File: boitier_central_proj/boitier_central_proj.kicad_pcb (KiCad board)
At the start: 2 copper layers, 50 x 50 mm, 11 parts, among them J1 Conn_01x02_Pin, J2 Conn_01x03_Pin, J4 Conn_01x02_Pin, Q1 IRLZ34N, U1 XIAO-nRF52840-SMD

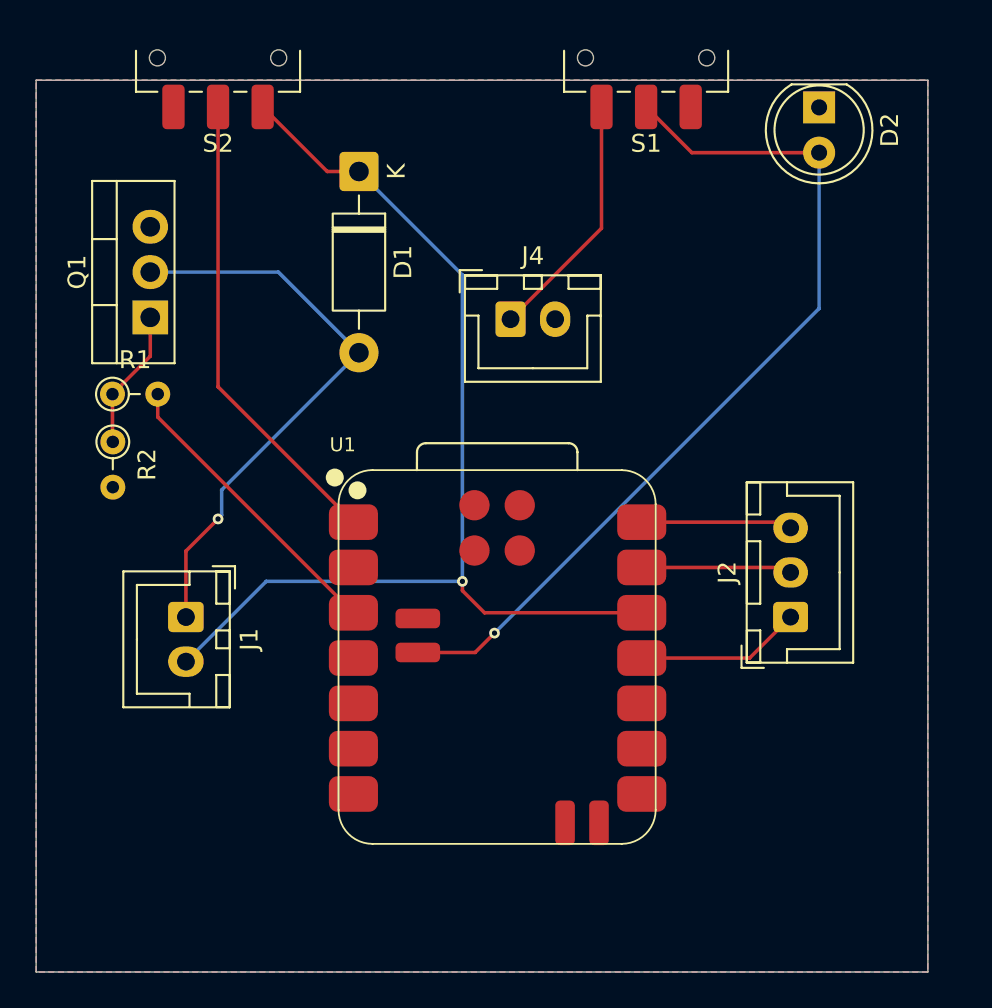
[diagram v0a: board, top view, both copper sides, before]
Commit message: Ajout du 3d duseeduiino et du tp4056 + ajout des trous
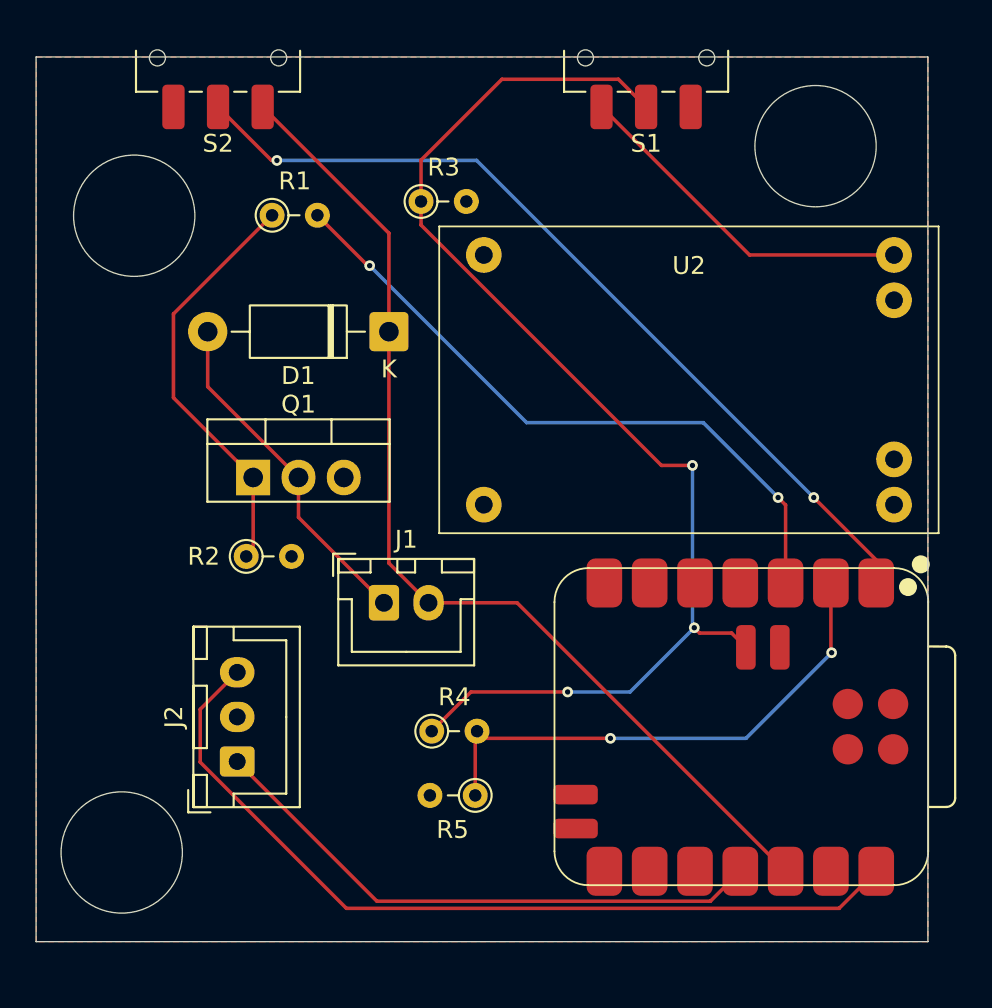
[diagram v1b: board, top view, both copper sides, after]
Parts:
- removed D2: LED, LED_THT:LED_D5.0mm
- removed J4: Conn_01x02_Pin, Connector_JST:JST_XH_B2B-XH-A_1x02_P2.50mm_Vertical
- added R3: 1k, Resistor_THT:R_Axial_DIN0204_L3.6mm_D1.6mm_P2.54mm_Vertical, F.Cu at (73.6, 36.8)
- added R4: 1k, Resistor_THT:R_Axial_DIN0204_L3.6mm_D1.6mm_P2.54mm_Vertical, F.Cu at (74.2, 66.5)
- added R5: 1k, Resistor_THT:R_Axial_DIN0204_L3.6mm_D1.6mm_P2.54mm_Vertical, F.Cu at (76.6, 70.1)
- added U2: ~, TP4056:TP4056, F.Cu at (74.6, 55.4)
- R2: value 1k -> 10k
- moved J2 32.1 mm to (63.3, 68.2)
- moved U1 14.1 mm to (91.5, 66.3), turned to -90 degrees
- moved R1 13.4 mm to (65.2, 37.6)
- moved J1 11.1 mm to (71.5, 59.3), turned to 0 degrees
- moved Q1 10.7 mm to (64.2, 52.3), turned to 0 degrees
- moved R2 9.86 mm to (63.8, 56.7), turned to 0 degrees
- moved D1 9.14 mm to (71.8, 44.1), turned to 180 degrees
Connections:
- S1 pad 3: Net-(J4-Pin_1) -> /OUT+
- U1 pad 2: unconnected-(U1-P0.03_A1_D1-Pad2) -> /BAT_level
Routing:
- net /LEDS+: track 8.48 -> 48.1 mm
- net /BAT_level: track 0.00 -> 29.6 mm, vias 0 -> 2
- net /LEDS_C: track 9.30 -> 32.1 mm
- net /Arme_Selection: track 26.4 -> 48.7 mm, vias 0 -> 2
- net /moteur_c: track 16.8 -> 37.3 mm, vias 0 -> 2
- net /OUT+: track 0.00 -> 19.8 mm
- net /BAT+: track 50.0 -> 69.4 mm, vias 1 -> 3
- net Net-(Q1-G): track 7.87 -> 23.4 mm
- net Net-(J4-Pin_1): track 14.0 -> 0.00 mm
- net Net-(D1-A): track 32.4 -> 19.3 mm, vias 1 -> 0
- net GND: track 8.50 -> 0.00 mm
- net /3V3: track 60.7 -> 57.9 mm, vias 1 -> 0
- removed copper zone on B.Cu, net GND
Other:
- board size 50 x 50 mm -> 50 x 49.6 mm

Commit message: Presque pret a etre produit
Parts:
- added D2: LED, LED_THT:LED_D5.0mm, F.Cu at (73.5, 32.5)
- moved R2 14.2 mm to (68.6, 70.1)
- moved Q1 10.7 mm to (53.9, 49.1), turned to -90 degrees
- moved R3 9.23 mm to (82.7, 35.5), turned to 180 degrees
- moved D1 5.81 mm to (66.0, 43.8)
- moved J2 4.10 mm to (59.9, 65.9)
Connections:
- S1 pad 1: GND -> unconnected-(S1-Pad1)
- U1 pad 22: unconnected-(U1-GND-Pad22) -> GND
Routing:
- net Net-(Q1-G): track 23.4 -> 44.6 mm, vias 0 -> 3
- net Net-(D1-A): track 19.3 -> 31.1 mm
- net /BAT+: track 69.4 -> 57.9 mm
- net Net-(D2-A): track 0.00 -> 5.42 mm
- net /LEDS_C: track 32.1 -> 36.5 mm
- net /LEDS+: track 48.1 -> 51.7 mm
- net /3V3: track 57.9 -> 59.5 mm
- added copper zone on B.Cu, net GND

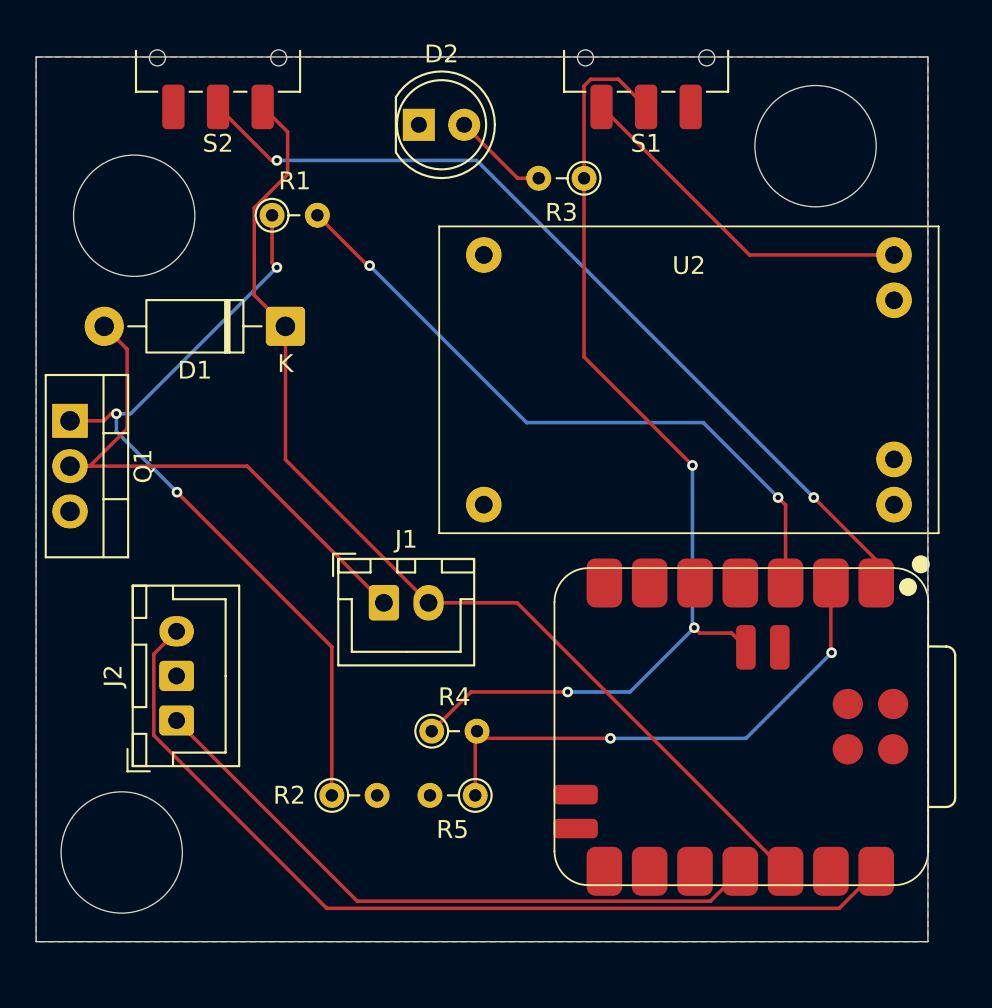
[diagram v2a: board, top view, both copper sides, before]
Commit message: Modification des trous pour le support + ajout des 3d + correction de la position du TP4056
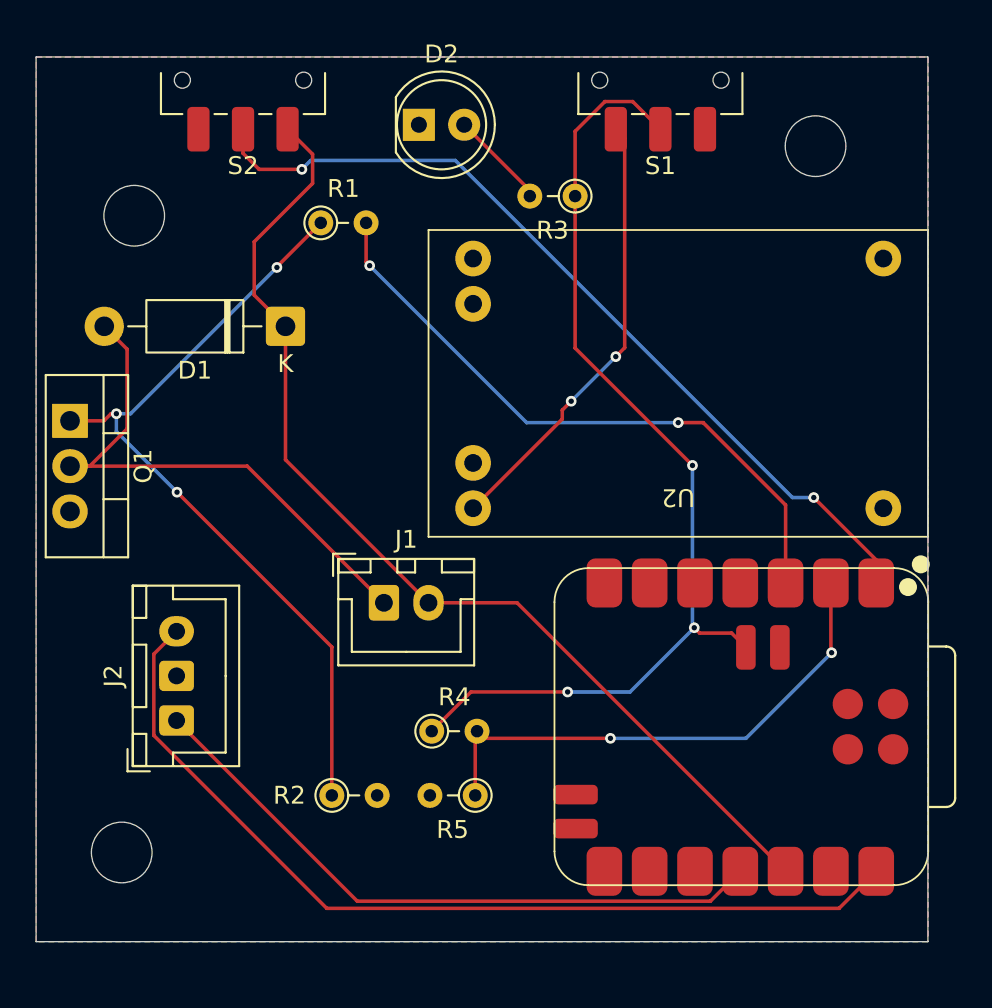
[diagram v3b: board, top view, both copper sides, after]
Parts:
- moved U2 32.2 mm to (102.0, 38.4), turned to 180 degrees
- moved R1 2.76 mm to (68.0, 38.0)
- moved S2 1.88 mm to (63.6, 30.0)
- moved S1 1.48 mm to (87.0, 30.0)
- moved R3 1.12 mm to (82.2, 36.5)
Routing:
- net /OUT+: track 19.8 -> 25.0 mm, vias 0 -> 2
- net /moteur_c: track 37.3 -> 35.8 mm
- net /Arme_Selection: track 48.7 -> 48.0 mm
- net /3V3: track 59.5 -> 58.8 mm
- net /BAT+: track 57.9 -> 57.4 mm
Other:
- outline, holes or cut-outs redrawn
